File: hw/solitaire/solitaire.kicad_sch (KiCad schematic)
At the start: 16 parts, among them J1 FFC2B35-10-T, J3 SBW, J4 BATT_IN, SW1 DEAL, SW2 UNDO, SW3 SKQUCAA010, U1 TPS63900, U2 MSP430FR2355TDBTR

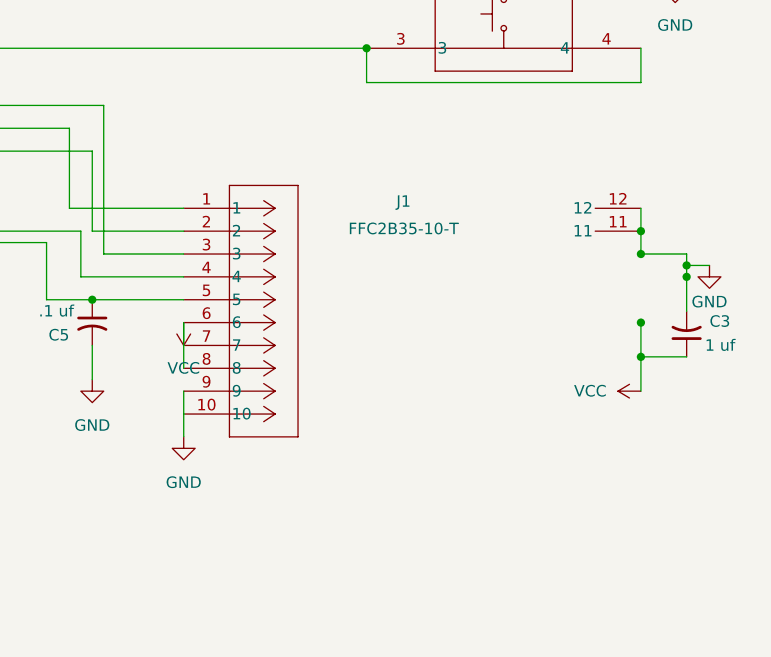
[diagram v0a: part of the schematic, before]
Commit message: Revert "Replace obsolete Molex 51441-1093 with GCT FFC2B35-10-T at J1"
This reverts commit c108aca33e9456606b33d22a310b62a8a5f5fa6a.
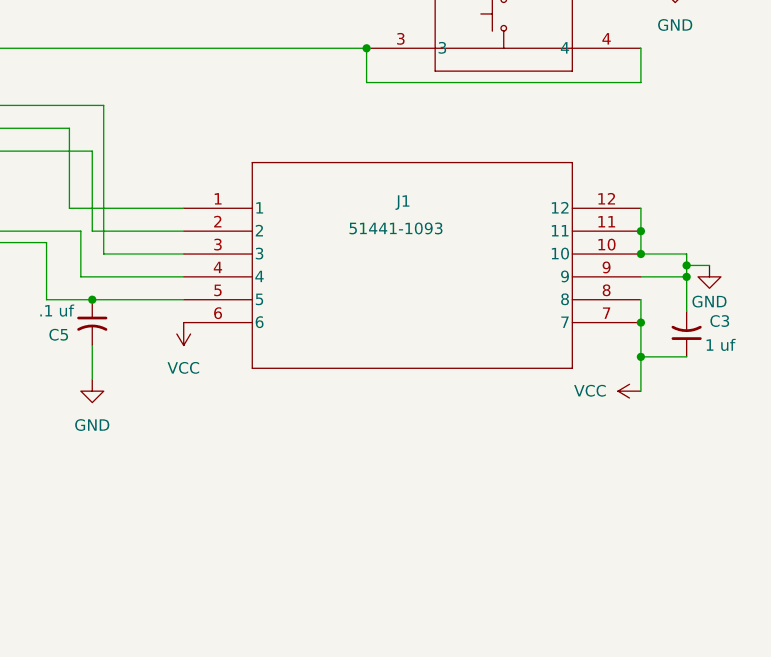
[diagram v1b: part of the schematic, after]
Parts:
- J1: value FFC2B35-10-T -> 51441-1093; footprint FFC2B35_10_T:CONN_FFC2B35-10-x_GCT -> 514411093:CON10_1X10_DRB_51441_MOL; symbol FFC2B35_10_T:FFC2B35-10-T -> 514411093:514411093
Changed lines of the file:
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@@
-	(wire
-		(pts
-			(xy 222.25 101.6) (xy 222.25 104.14)
-		)
-		(stroke
-			(width 0)
-			(type default)
-		)
-	)
-	(wire
-		(pts
-			(xy 222.25 104.14) (xy 222.25 106.68)
-		)
-		(stroke
-			(width 0)
-			(type default)
-		)
-	)
-	(wire
-		(pts
-			(xy 222.25 109.22) (xy 222.25 111.76)
-		)
-		(stroke
-			(width 0)
-			(type default)
-		)
-	)
-	(wire
-		(pts
-			(xy 222.25 111.76) (xy 222.25 114.3)
-		)
-		(stroke
-			(width 0)
-			(type default)
-		)
-	)
 	(wire
 		(pts
@@
 		(pts
 			(xy 213.36 77.47) (xy 213.36 93.98)
+		)
+		(stroke
+			(width 0)
+			(type default)
+		)
+	)
+	(wire
+		(pts
+			(xy 273.05 99.06) (xy 273.05 101.6)
 		)
 		(stroke
@@
 	(wire
 		(pts
+			(xy 273.05 96.52) (xy 278.13 96.52)
+		)
+		(stroke
+			(width 0)
+			(type default)
+		)
+	)
+	(wire
+		(pts
 			(xy 276.86 59.69) (xy 276.86 63.5)
 		)
@@
 	(symbol
 		(lib_id "power:GND")
-		(at 222.25 114.3 0)
-		(unit 1)
-		(exclude_from_sim no)
-		(in_bom yes)
-		(on_board yes)
-		(dnp no)
-		(fields_autoplaced yes)
-		(property "Reference" "#PWR019"
-			(at 222.25 120.65 0)
-			(effects
-				(font
-					(size 1.27 1.27)
-				)
-				(hide yes)
-			)
-		)
-		(property "Value" "GND"
-			(at 222.25 119.38 0)
-			(effects
-				(font
-					(size 1.27 1.27)
-				)
-			)
-		)
-		(property "Footprint" ""
-			(at 222.25 114.3 0)
-			(effects
-				(font
-					(size 1.27 1.27)
-				)
-				(hide yes)
-			)
-		)
-		(property "Datasheet" ""
-			(at 222.25 114.3 0)
-			(effects
-				(font
-					(size 1.27 1.27)
-				)
-				(hide yes)
-			)
-		)
-		(property "Description" "Power symbol creates a global label with name \"GND\" , ground"
-			(at 222.25 114.3 0)
-			(effects
-				(font
-					(size 1.27 1.27)
-				)
-				(hide yes)
-			)
-		)
-		(pin "1"
-		)
-		(instances
-			(project ""
-				(path "/37bed383-82de-493d-be12-9430e997c33d"
-					(reference "#PWR019")
-					(unit 1)
-				)
-			)
-		)
-	)
-	(symbol
-		(lib_id "power:GND")
 		(at 193.04 48.26 0)
 		(unit 1)
@@
 	)
 	(symbol
-		(lib_id "FFC2B35_10_T:FFC2B35-10-T")
+		(lib_id "514411093:514411093")
 		(at 222.25 88.9 0)
 		(unit 1)
@@
 			)
 		)
-		(property "Value" "FFC2B35-10-T"
+		(property "Value" "51441-1093"
 			(at 240.538 91.186 0)
 			(effects
@@
 			)
 		)
-		(property "Footprint" "FFC2B35_10_T:CONN_FFC2B35-10-x_GCT"
+		(property "Footprint" "514411093:CON10_1X10_DRB_51441_MOL"
 			(at 222.25 88.9 0)
 			(effects
@@
 			)
 		)
-		(property "Datasheet" "FFC2B35-10-T"
+		(property "Datasheet" "514411093"
 			(at 222.25 88.9 0)
 			(effects
@@
 			)
 		)
-		(property "Description" "GCT FFC2B35-10-T, 10-position 0.5mm pitch bottom-contact front-flip FPC/FFC connector - replacement for obsolete Molex 51441-1093"
+		(property "Description" "Molex 51441-1093, 10-position 0.5mm pitch bottom-contact FPC/FFC connector"
 			(at 222.25 88.9 0)
 			(effects
